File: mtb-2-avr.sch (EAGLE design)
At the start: 18 parts, among them IC1 MEGA8A-AU, Q1/2 14.745 MHz, Q2 14.745 MHz

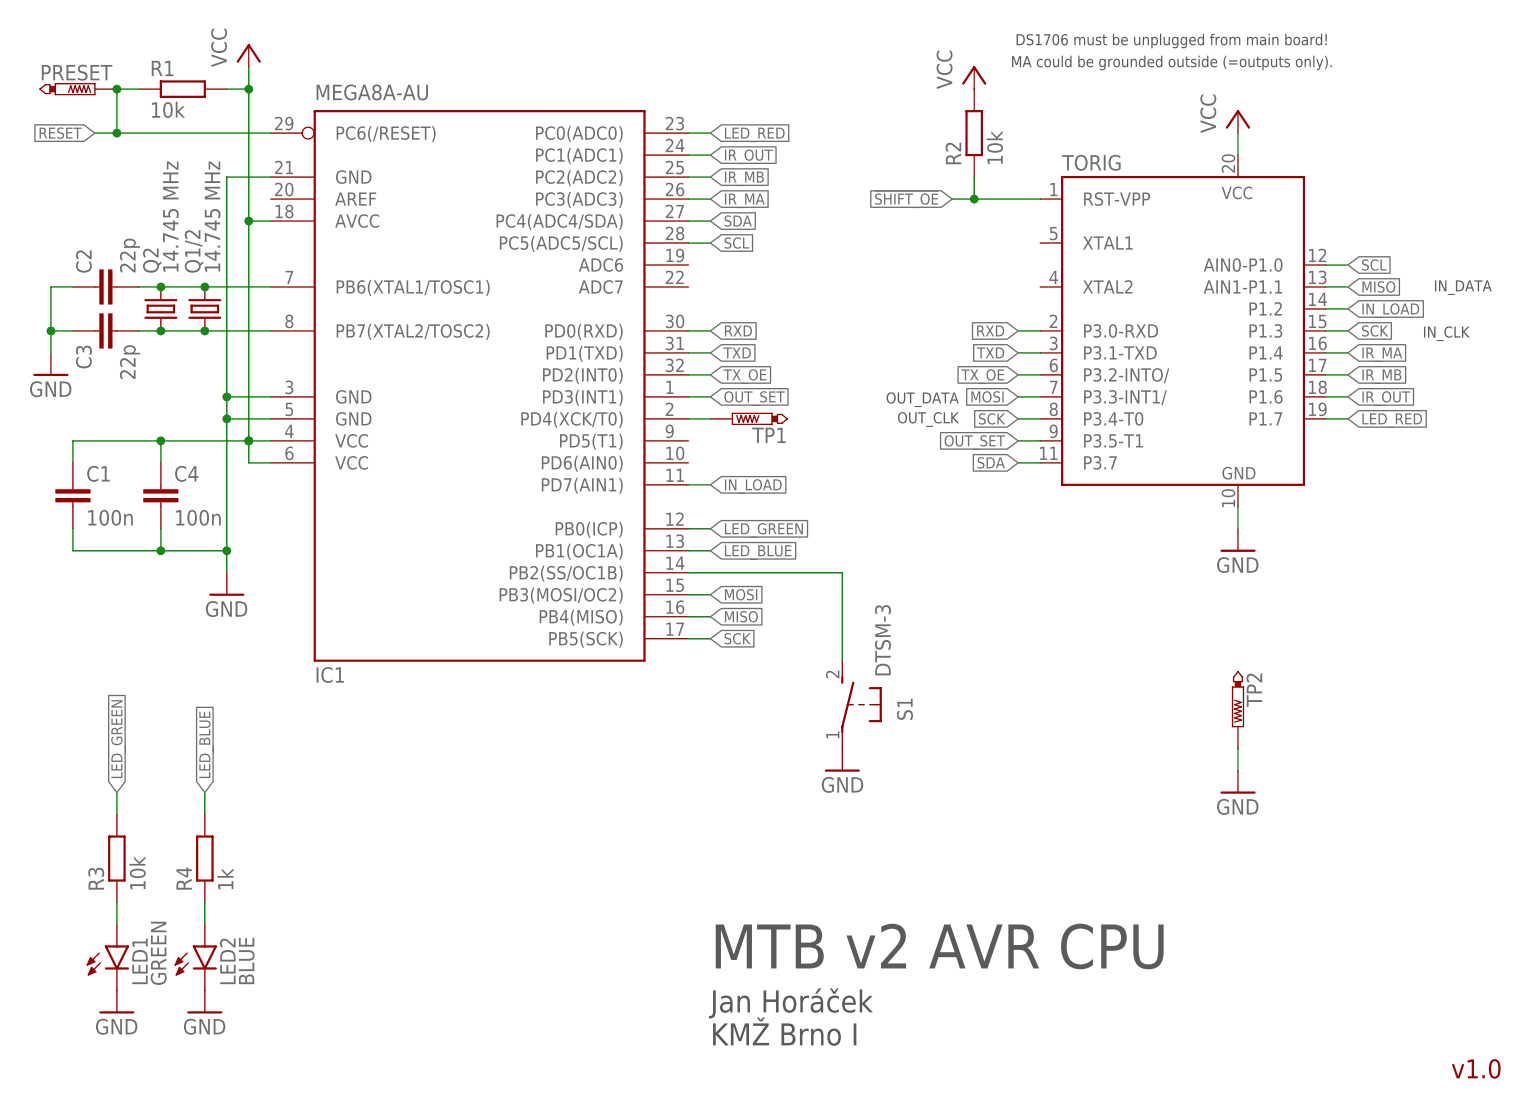
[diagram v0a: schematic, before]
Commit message: Free PB2, connect SHIFT_OE.
PB2 must be free because SPI uses it. Disconnected SHIFT_OE was bug.
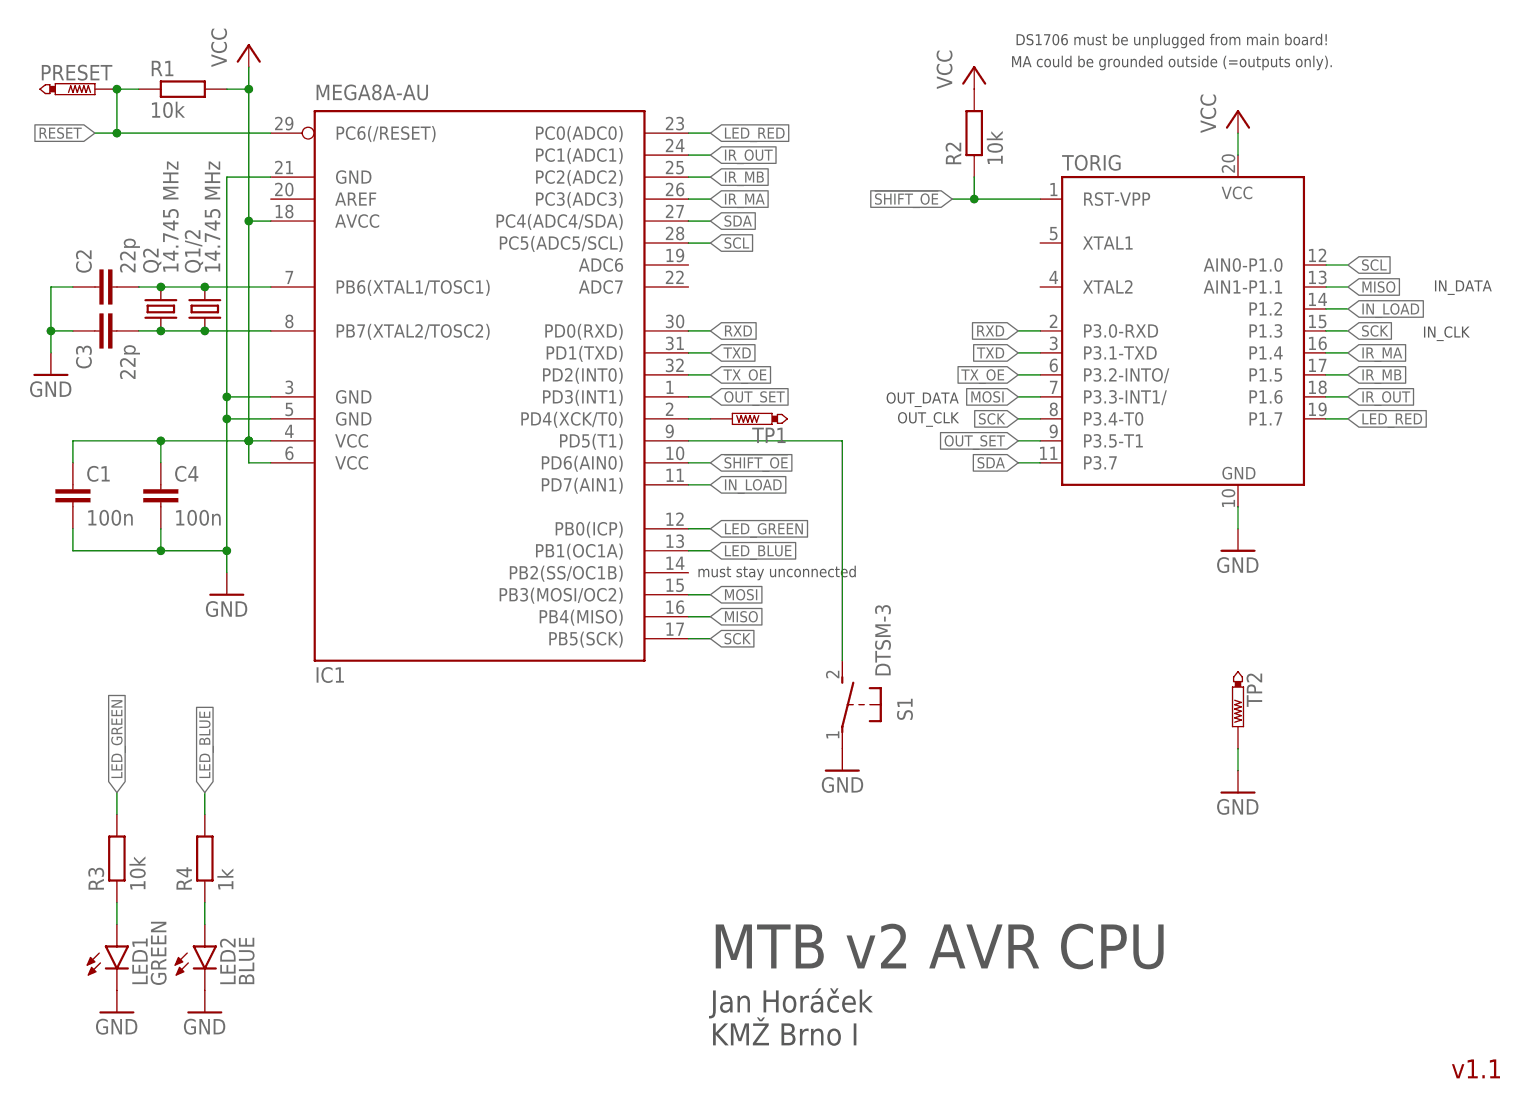
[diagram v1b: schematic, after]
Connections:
- removed net N$5: IC1.PB2(SS/OC1B), S1.2
- new net BTN: IC1.PD5(T1), S1.2
- net !SHIFT_OE: now also IC1.PD6(AIN0)
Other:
- note added: "must stay unconnected"
- note added: "v1.1"
- note removed: "v1.0"
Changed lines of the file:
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@@
 <grid distance="0.1" unitdist="inch" unit="mm" style="lines" multiple="1" display="no" altdistance="0.01" altunitdist="inch" altunit="mm"/>
 <layers>
-<layer number="1" name="Top" color="3" fill="1" visible="yes" active="no"/>
-<layer number="2" name="Route2" color="16" fill="1" visible="yes" active="no"/>
-<layer number="3" name="Route3" color="17" fill="1" visible="yes" active="no"/>
-<layer number="4" name="Route4" color="18" fill="1" visible="yes" active="no"/>
-<layer number="5" name="Route5" color="19" fill="1" visible="yes" active="no"/>
-<layer number="6" name="Route6" color="25" fill="1" visible="yes" active="no"/>
-<layer number="7" name="Route7" color="26" fill="1" visible="yes" active="no"/>
-<layer number="8" name="Route8" color="27" fill="1" visible="yes" active="no"/>
-<layer number="9" name="Route9" color="28" fill="1" visible="yes" active="no"/>
-<layer number="10" name="Route10" color="29" fill="1" visible="yes" active="no"/>
-<layer number="11" name="Route11" color="30" fill="1" visible="yes" active="no"/>
-<layer number="12" name="Route12" color="20" fill="1" visible="yes" active="no"/>
-<layer number="13" name="Route13" color="21" fill="1" visible="yes" active="no"/>
-<layer number="14" name="Route14" color="22" fill="1" visible="yes" active="no"/>
-<layer number="15" name="Route15" color="23" fill="1" visible="yes" active="no"/>
-<layer number="16" name="Bottom" color="4" fill="1" visible="yes" active="no"/>
-<layer number="17" name="Pads" color="2" fill="1" visible="yes" active="no"/>
-<layer number="18" name="Vias" color="2" fill="1" visible="yes" active="no"/>
-<layer number="19" name="Unrouted" color="6" fill="1" visible="yes" active="no"/>
-<layer number="20" name="Dimension" color="24" fill="1" visible="yes" active="no"/>
-<layer number="21" name="tPlace" color="7" fill="1" visible="yes" active="no"/>
-<layer number="22" name="bPlace" color="7" fill="1" visible="yes" active="no"/>
-<layer number="23" name="tOrigins" color="15" fill="1" visible="yes" active="no"/>
-<layer number="24" name="bOrigins" color="15" fill="1" visible="yes" active="no"/>
-<layer number="25" name="tNames" color="7" fill="1" visible="yes" active="no"/>
-<layer number="26" name="bNames" color="7" fill="1" visible="yes" active="no"/>
-<layer number="27" name="tValues" color="7" fill="1" visible="yes" active="no"/>
-<layer number="28" name="bValues" color="7" fill="1" visible="yes" active="no"/>
+<layer number="1" name="Top" color="3" fill="1" visible="no" active="no"/>
+<layer number="2" name="Route2" color="16" fill="1" visible="no" active="no"/>
+<layer number="3" name="Route3" color="17" fill="1" visible="no" active="no"/>
+<layer number="4" name="Route4" color="18" fill="1" visible="no" active="no"/>
+<layer number="5" name="Route5" color="19" fill="1" visible="no" active="no"/>
+<layer number="6" name="Route6" color="25" fill="1" visible="no" active="no"/>
+<layer number="7" name="Route7" color="26" fill="1" visible="no" active="no"/>
+<layer number="8" name="Route8" color="27" fill="1" visible="no" active="no"/>
+<layer number="9" name="Route9" color="28" fill="1" visible="no" active="no"/>
+<layer number="10" name="Route10" color="29" fill="1" visible="no" active="no"/>
+<layer number="11" name="Route11" color="30" fill="1" visible="no" active="no"/>
+<layer number="12" name="Route12" color="20" fill="1" visible="no" active="no"/>
+<layer number="13" name="Route13" color="21" fill="1" visible="no" active="no"/>
+<layer number="14" name="Route14" color="22" fill="1" visible="no" active="no"/>
+<layer number="15" name="Route15" color="23" fill="1" visible="no" active="no"/>
+<layer number="16" name="Bottom" color="4" fill="1" visible="no" active="no"/>
+<layer number="17" name="Pads" color="2" fill="1" visible="no" active="no"/>
+<layer number="18" name="Vias" color="2" fill="1" visible="no" active="no"/>
+<layer number="19" name="Unrouted" color="6" fill="1" visible="no" active="no"/>
+<layer number="20" name="Dimension" color="24" fill="1" visible="no" active="no"/>
+<layer number="21" name="tPlace" color="7" fill="1" visible="no" active="no"/>
+<layer number="22" name="bPlace" color="7" fill="1" visible="no" active="no"/>
+<layer number="23" name="tOrigins" color="15" fill="1" visible="no" active="no"/>
+<layer number="24" name="bOrigins" color="15" fill="1" visible="no" active="no"/>
+<layer number="25" name="tNames" color="7" fill="1" visible="no" active="no"/>
+<layer number="26" name="bNames" color="7" fill="1" visible="no" active="no"/>
+<layer number="27" name="tValues" color="7" fill="1" visible="no" active="no"/>
+<layer number="28" name="bValues" color="7" fill="1" visible="no" active="no"/>
 <layer number="29" name="tStop" color="7" fill="3" visible="no" active="no"/>
 <layer number="30" name="bStop" color="7" fill="6" visible="no" active="no"/>
@@
 <layer number="35" name="tGlue" color="7" fill="4" visible="no" active="no"/>
 <layer number="36" name="bGlue" color="7" fill="5" visible="no" active="no"/>
-<layer number="37" name="tTest" color="7" fill="1" visible="yes" active="no"/>
-<layer number="38" name="bTest" color="7" fill="1" visible="yes" active="no"/>
+<layer number="37" name="tTest" color="7" fill="1" visible="no" active="no"/>
+<layer number="38" name="bTest" color="7" fill="1" visible="no" active="no"/>
 <layer number="39" name="tKeepout" color="4" fill="11" visible="no" active="no"/>
 <layer number="40" name="bKeepout" color="1" fill="11" visible="no" active="no"/>
@@
 <layer number="44" name="Drills" color="7" fill="1" visible="no" active="no"/>
 <layer number="45" name="Holes" color="7" fill="1" visible="no" active="no"/>
-<layer number="46" name="Milling" color="3" fill="1" visible="yes" active="no"/>
-<layer number="47" name="Measures" color="7" fill="1" visible="yes" active="no"/>
-<layer number="48" name="Document" color="7" fill="1" visible="yes" active="no"/>
-<layer number="49" name="Reference" color="7" fill="1" visible="yes" active="no"/>
-<layer number="50" name="dxf" color="7" fill="1" visible="yes" active="no"/>
-<layer number="51" name="tDocu" color="7" fill="1" visible="yes" active="no"/>
-<layer number="52" name="bDocu" color="7" fill="1" visible="yes" active="no"/>
-<layer number="53" name="tGND_GNDA" color="7" fill="9" visible="yes" active="no"/>
-<layer number="54" name="bGND_GNDA" color="1" fill="9" visible="yes" active="no"/>
-<layer number="56" name="wert" color="7" fill="1" visible="yes" active="no"/>
-<layer number="57" name="tCAD" color="7" fill="1" visible="yes" active="no"/>
-<layer number="59" name="tCarbon" color="7" fill="1" visible="yes" active="no"/>
-<layer number="60" name="bCarbon" color="7" fill="1" visible="yes" active="no"/>
+<layer number="46" name="Milling" color="3" fill="1" visible="no" active="no"/>
+<layer number="47" name="Measures" color="7" fill="1" visible="no" active="no"/>
+<layer number="48" name="Document" color="7" fill="1" visible="no" active="no"/>
+<layer number="49" name="Reference" color="7" fill="1" visible="no" active="no"/>
+<layer number="50" name="dxf" color="7" fill="1" visible="no" active="no"/>
+<layer number="51" name="tDocu" color="7" fill="1" visible="no" active="no"/>
+<layer number="52" name="bDocu" color="7" fill="1" visible="no" active="no"/>
+<layer number="53" name="tGND_GNDA" color="7" fill="9" visible="no" active="no"/>
+<layer number="54" name="bGND_GNDA" color="1" fill="9" visible="no" active="no"/>
+<layer number="56" name="wert" color="7" fill="1" visible="no" active="no"/>
+<layer number="57" name="tCAD" color="7" fill="1" visible="no" active="no"/>
+<layer number="59" name="tCarbon" color="7" fill="1" visible="no" active="no"/>
+<layer number="60" name="bCarbon" color="7" fill="1" visible="no" active="no"/>
 <layer number="88" name="SimResults" color="9" fill="1" visible="yes" active="yes"/>
 <layer number="89" name="SimProbes" color="9" fill="1" visible="yes" active="yes"/>
@@
 <text x="86.36" y="8.89" size="2.54" layer="97">Jan Horáček
 KMŽ Brno I</text>
-<text x="171.958" y="5.08" size="2.1844" layer="94">v1.0</text>
+<text x="171.958" y="5.08" size="2.1844" layer="94">v1.1</text>
 <text x="139.7" y="124.46" size="1.27" layer="97" align="bottom-center">DS1706 must be unplugged from main board!</text>
 <text x="139.7" y="121.92" size="1.27" layer="97" align="bottom-center">MA could be grounded outside (=outputs only).</text>
@@
 <text x="168.656" y="90.678" size="1.27" layer="97">IN_CLK</text>
 <text x="169.926" y="96.012" size="1.27" layer="97">IN_DATA</text>
+<text x="84.836" y="62.992" size="1.27" layer="97">must stay unconnected</text>
 </plain>
 <instances>
@@
 <junction x="116.84" y="106.68"/>
 </segment>
+<segment>
+<pinref part="IC1" gate="G$1" pin="PD6(AIN0)"/>
+<wire x1="83.82" y1="76.2" x2="86.36" y2="76.2" width="0.1524" layer="91"/>
+<label x="86.36" y="76.2" size="1.27" layer="95" xref="yes"/>
+</segment>
 </net>
 <net name="N$3" class="0">
@@
 </segment>
 </net>
-<net name="N$5" class="0">
+<net name="BTN" class="0">
 <segment>
 <pinref part="S1" gate="G$1" pin="2"/>
-<pinref part="IC1" gate="G$1" pin="PB2(SS/OC1B)"/>
-<wire x1="101.6" y1="63.5" x2="101.6" y2="53.34" width="0.1524" layer="91"/>
-<wire x1="83.82" y1="63.5" x2="101.6" y2="63.5" width="0.1524" layer="91"/>
-</segment>
-</net>
+<pinref part="IC1" gate="G$1" pin="PD5(T1)"/>
+<wire x1="83.82" y1="78.74" x2="101.6" y2="78.74" width="0.1524" layer="91"/>
+<wire x1="101.6" y1="78.74" x2="101.6" y2="53.34" width="0.1524" layer="91"/>
+</segment>
+</net>
